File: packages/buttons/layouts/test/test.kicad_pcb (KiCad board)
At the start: 2 copper layers, 8 parts

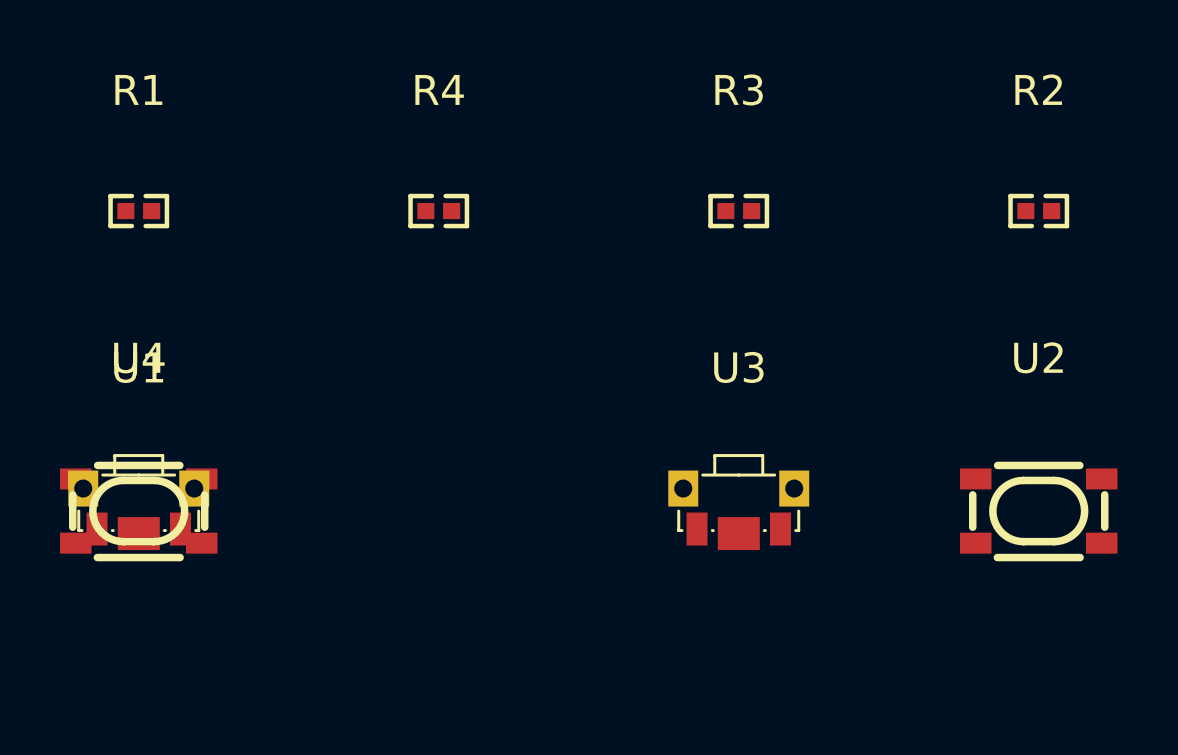
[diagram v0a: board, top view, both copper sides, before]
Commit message: update example and reademe
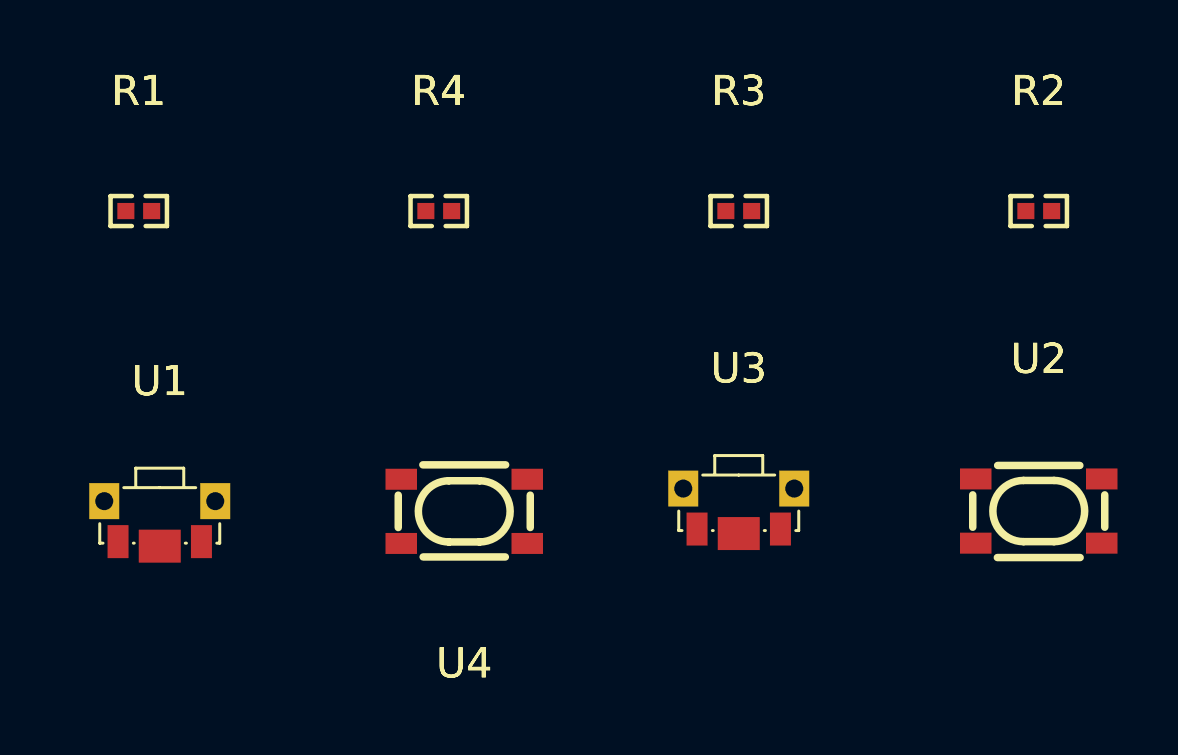
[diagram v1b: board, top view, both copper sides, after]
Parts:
- moved U4 10.9 mm to (10.8, 0.01), turned to 180 degrees
- moved U1 0.82 mm to (0.70, 0.42)
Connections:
- net btn_pullup_vertical-hv renamed hv
- R1 pad 1: net-2 -> net-3
- R2 pad 1: net-1 -> net
- R3 pad 1: net -> net-1
- R4 pad 1: net-3 -> net-2
- U1 pad 1: line -> line-3
- U1 pad 2: net-2 -> net-3
- U2 pad 1: line-3 -> line-1
- U2 pad 2: line-3 -> line-1
- U2 pad 3: net-1 -> net
- U2 pad 4: net-1 -> net
- U3 pad 1: line-2 -> line
- U3 pad 2: net -> net-1
- U4 pad 1: line-1 -> line-2
- U4 pad 2: line-1 -> line-2
- U4 pad 3: net-3 -> net-2
- U4 pad 4: net-3 -> net-2

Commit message: WIP
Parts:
- R1, R2, R3, R4: footprint atopile:R0402-56259e -> UNI_ROYAL_0402WGF1002TCE:R0402
- U1, U3: footprint atopile:KEY-SMD_SKTDLDE010-0426f5 -> ALPSALPINE_SKTDLDE010:KEY-SMD_SKTDLDE010
- U2, U4: footprint atopile:KEY-SMD_4P-L4.2-W3.2-P2.20-LS4.6-a2ccf0 -> ALPSALPINE_SKRPACE010:KEY-SMD_4P-L4.2-W3.2-P2.20-LS4.6
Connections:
- net net renamed _4
- net net-1 renamed _2
- net net-2 renamed unnamed[0]-1
- net net-3 renamed unnamed[0]
- U1 pad 1: line-3 -> line-1
- U2 pad 1: line-1 -> line
- U2 pad 2: line-1 -> line
- U3 pad 1: line -> line-3

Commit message: build all once
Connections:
- net _2 renamed net
- net _4 renamed net-2
- net unnamed[0] renamed net-1
- net unnamed[0]-1 renamed net-3
- U3 pad 1: line-3 -> line-2
- U4 pad 1: line-2 -> line-3
- U4 pad 2: line-2 -> line-3

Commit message: rebuild
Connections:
- net net-3 renamed _3
- R1 pad 1: net-1 -> _2
- R2 pad 1: net-2 -> net
- R3 pad 1: net -> net-1
- U1 pad 1: line-1 -> line-3
- U1 pad 2: net-1 -> _2
- U2 pad 1: line -> line-1
- U2 pad 2: line -> line-1
- U2 pad 3: net-2 -> net
- U2 pad 4: net-2 -> net
- U3 pad 2: net -> net-1
- U4 pad 1: line-3 -> line
- U4 pad 2: line-3 -> line
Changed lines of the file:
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@@
     (net 3 "btn_pulldown_horizontal.btn.footprint.pins[2].net-net")
     (net 4 "btn_pulldown_horizontal-gnd")
-    (net 5 "net-1")
+    (net 5 "_2")
     (net 6 "btn_pulldown_horizontal.btn.footprint.pins[3].net-net")
     (net 7 "btn_pullup_horizontal.btn.footprint.pins[3].net-net")
     (net 8 "line-2")
-    (net 9 "net")
-    (net 10 "line-1")
+    (net 9 "net-1")
+    (net 10 "line-3")
     (net 11 "btn_pullup_horizontal-hv")
     (net 12 "btn_pullup_horizontal.btn.footprint.pins[2].net-net")
-    (net 13 "net-2")
-    (net 14 "line")
-    (net 15 "line-3")
-    (net 16 "net-3")
+    (net 13 "net")
+    (net 14 "line-1")
+    (net 15 "line")
+    (net 16 "_3")
     (footprint "UNI_ROYAL_0402WGF1002TCE:R0402"
         (layer "F.Cu")
@@
             (size 0.57 0.54)
             (layers "F.Cu" "F.Paste" "F.Mask")
-            (net 9 "net")
+            (net 9 "net-1")
         )
         (model "${KIPRJMOD}/../../parts/UNI_ROYAL_0402WGF1002TCE/R0402_L1.0-W0.5-H0.4.step"
@@
             (size 0.7 1.1)
             (layers "F.Cu" "F.Paste" "F.Mask")
-            (net 9 "net")
+            (net 9 "net-1")
         )
         (pad "1" smd rect
@@
             (size 1.05 0.7)
             (layers "F.Cu" "F.Paste" "F.Mask")
-            (net 14 "line")
+            (net 14 "line-1")
         )
         (pad "2" smd rect
@@
             (size 1.05 0.7)
             (layers "F.Cu" "F.Paste" "F.Mask")
-            (net 14 "line")
+            (net 14 "line-1")
         )
         (pad "3" smd rect
@@
             (size 1.05 0.7)
             (layers "F.Cu" "F.Paste" "F.Mask")
-            (net 13 "net-2")
+            (net 13 "net")
         )
         (pad "4" smd rect
@@
             (size 1.05 0.7)
             (layers "F.Cu" "F.Paste" "F.Mask")
-            (net 13 "net-2")
+            (net 13 "net")
         )
         (model "${KIPRJMOD}/../../parts/ALPSALPINE_SKRPACE010/KEY-SMD_4P-L4.2-W3.2-H2.5-LS4.6-P2.2.step"
@@
             (size 0.57 0.54)
             (layers "F.Cu" "F.Paste" "F.Mask")
-            (net 16 "net-3")
+            (net 16 "_3")
         )
         (model "${KIPRJMOD}/../../parts/UNI_ROYAL_0402WGF1002TCE/R0402_L1.0-W0.5-H0.4.step"
@@
             (size 0.7 1.1)
             (layers "F.Cu" "F.Paste" "F.Mask")
-            (net 5 "net-1")
+            (net 5 "_2")
         )
         (pad "1" smd rect
@@
             (size 0.7 1.1)
             (layers "F.Cu" "F.Paste" "F.Mask")
-            (net 10 "line-1")
+            (net 10 "line-3")
         )
         (pad "3" smd rect
@@
             (size 0.57 0.54)
             (layers "F.Cu" "F.Paste" "F.Mask")
-            (net 13 "net-2")
+            (net 13 "net")
         )
         (model "${KIPRJMOD}/../../parts/UNI_ROYAL_0402WGF1002TCE/R0402_L1.0-W0.5-H0.4.step"
@@
             (size 1.05 0.7)
             (layers "F.Cu" "F.Paste" "F.Mask")
-            (net 15 "line-3")
+            (net 15 "line")
         )
         (pad "2" smd rect
@@
             (size 1.05 0.7)
             (layers "F.Cu" "F.Paste" "F.Mask")
-            (net 15 "line-3")
+            (net 15 "line")
         )
         (pad "3" smd rect
@@
             (size 1.05 0.7)
             (layers "F.Cu" "F.Paste" "F.Mask")
-            (net 16 "net-3")
+            (net 16 "_3")
         )
         (pad "4" smd rect
@@
             (size 1.05 0.7)
             (layers "F.Cu" "F.Paste" "F.Mask")
-            (net 16 "net-3")
+            (net 16 "_3")
         )
         (model "${KIPRJMOD}/../../parts/ALPSALPINE_SKRPACE010/KEY-SMD_4P-L4.2-W3.2-H2.5-LS4.6-P2.2.step"
@@
             (size 0.57 0.54)
             (layers "F.Cu" "F.Paste" "F.Mask")
-            (net 5 "net-1")
+            (net 5 "_2")
         )
         (model "${KIPRJMOD}/../../parts/UNI_ROYAL_0402WGF1002TCE/R0402_L1.0-W0.5-H0.4.step"

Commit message: add build_all.py
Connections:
- R3 pad 1: net-1 -> unnamed[1]
- R4 pad 1: _3 -> net-1
- U1 pad 1: line-3 -> line-2
- U2 pad 1: line-1 -> line
- U2 pad 2: line-1 -> line
- U3 pad 1: line-2 -> line-3
- U3 pad 2: net-1 -> unnamed[1]
- U4 pad 1: line -> line-1
- U4 pad 2: line -> line-1
- U4 pad 3: _3 -> net-1
- U4 pad 4: _3 -> net-1
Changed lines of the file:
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@@
     (net 6 "btn_pulldown_horizontal.btn.footprint.pins[3].net-net")
     (net 7 "btn_pullup_horizontal.btn.footprint.pins[3].net-net")
-    (net 8 "line-2")
-    (net 9 "net-1")
-    (net 10 "line-3")
+    (net 8 "line-3")
+    (net 9 "unnamed[1]")
+    (net 10 "line-2")
     (net 11 "btn_pullup_horizontal-hv")
     (net 12 "btn_pullup_horizontal.btn.footprint.pins[2].net-net")
     (net 13 "net")
-    (net 14 "line-1")
-    (net 15 "line")
-    (net 16 "_3")
+    (net 14 "line")
+    (net 15 "line-1")
+    (net 16 "net-1")
     (footprint "UNI_ROYAL_0402WGF1002TCE:R0402"
         (layer "F.Cu")
@@
             (size 0.57 0.54)
             (layers "F.Cu" "F.Paste" "F.Mask")
-            (net 9 "net-1")
+            (net 9 "unnamed[1]")
         )
         (model "${KIPRJMOD}/../../parts/UNI_ROYAL_0402WGF1002TCE/R0402_L1.0-W0.5-H0.4.step"
@@
             (size 0.7 1.1)
             (layers "F.Cu" "F.Paste" "F.Mask")
-            (net 9 "net-1")
+            (net 9 "unnamed[1]")
         )
         (pad "1" smd rect
@@
             (size 0.7 1.1)
             (layers "F.Cu" "F.Paste" "F.Mask")
-            (net 8 "line-2")
+            (net 8 "line-3")
         )
         (pad "3" smd rect
@@
             (size 1.05 0.7)
             (layers "F.Cu" "F.Paste" "F.Mask")
-            (net 14 "line-1")
+            (net 14 "line")
         )
         (pad "2" smd rect
@@
             (size 1.05 0.7)
             (layers "F.Cu" "F.Paste" "F.Mask")
-            (net 14 "line-1")
+            (net 14 "line")
         )
         (pad "3" smd rect
@@
             (size 0.57 0.54)
             (layers "F.Cu" "F.Paste" "F.Mask")
-            (net 16 "_3")
+            (net 16 "net-1")
         )
         (model "${KIPRJMOD}/../../parts/UNI_ROYAL_0402WGF1002TCE/R0402_L1.0-W0.5-H0.4.step"
@@
             (size 0.7 1.1)
             (layers "F.Cu" "F.Paste" "F.Mask")
-            (net 10 "line-3")
+            (net 10 "line-2")
         )
         (pad "3" smd rect
@@
             (size 1.05 0.7)
             (layers "F.Cu" "F.Paste" "F.Mask")
-            (net 15 "line")
+            (net 15 "line-1")
         )
         (pad "2" smd rect
@@
             (size 1.05 0.7)
             (layers "F.Cu" "F.Paste" "F.Mask")
-            (net 15 "line")
+            (net 15 "line-1")
         )
         (pad "3" smd rect
@@
             (size 1.05 0.7)
             (layers "F.Cu" "F.Paste" "F.Mask")
-            (net 16 "_3")
+            (net 16 "net-1")
         )
         (pad "4" smd rect
@@
             (size 1.05 0.7)
             (layers "F.Cu" "F.Paste" "F.Mask")
-            (net 16 "_3")
+            (net 16 "net-1")
         )
         (model "${KIPRJMOD}/../../parts/ALPSALPINE_SKRPACE010/KEY-SMD_4P-L4.2-W3.2-H2.5-LS4.6-P2.2.step"

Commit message: update with 3d models
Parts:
- R1, R2, R3, R4: footprint UNI_ROYAL_0402WGF1002TCE:R0402 -> atopile:R0402-56259e
- U1, U3: footprint ALPSALPINE_SKTDLDE010:KEY-SMD_SKTDLDE010 -> atopile:KEY-SMD_SKTDLDE010-0426f5
- U2, U4: footprint ALPSALPINE_SKRPACE010:KEY-SMD_4P-L4.2-W3.2-P2.20-LS4.6 -> atopile:KEY-SMD_4P-L4.2-W3.2-P2.20-LS4.6-a2ccf0
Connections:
- R1 pad 1: _2 -> net
- R2 pad 1: net -> net-2
- R3 pad 1: unnamed[1] -> net-1
- R4 pad 1: net-1 -> net-3
- U1 pad 1: line-2 -> line
- U1 pad 2: _2 -> net
- U2 pad 1: line -> line-1
- U2 pad 2: line -> line-1
- U2 pad 3: net -> net-2
- U2 pad 4: net -> net-2
- U3 pad 2: unnamed[1] -> net-1
- U4 pad 1: line-1 -> line-2
- U4 pad 2: line-1 -> line-2
- U4 pad 3: net-1 -> net-3
- U4 pad 4: net-1 -> net-3
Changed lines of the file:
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@@
     (net 3 "btn_pulldown_horizontal.btn.footprint.pins[2].net-net")
     (net 4 "btn_pulldown_horizontal-gnd")
-    (net 5 "_2")
+    (net 5 "net")
     (net 6 "btn_pulldown_horizontal.btn.footprint.pins[3].net-net")
     (net 7 "btn_pullup_horizontal.btn.footprint.pins[3].net-net")
     (net 8 "line-3")
-    (net 9 "unnamed[1]")
-    (net 10 "line-2")
+    (net 9 "net-1")
+    (net 10 "line")
     (net 11 "btn_pullup_horizontal-hv")
     (net 12 "btn_pullup_horizontal.btn.footprint.pins[2].net-net")
-    (net 13 "net")
-    (net 14 "line")
-    (net 15 "line-1")
-    (net 16 "net-1")
-    (footprint "UNI_ROYAL_0402WGF1002TCE:R0402"
+    (net 13 "net-2")
+    (net 14 "line-1")
+    (net 15 "line-2")
+    (net 16 "net-3")
+    (footprint "atopile:R0402-56259e"
         (layer "F.Cu")
         (at 20 -10 0)
@@
             )
         )
-        (property "__atopile_lib_fp_hash__" "e8f2e4ec-73af-bd41-8630-d0c87c36316a"
+        (property "__atopile_lib_fp_hash__" "15bb07f0-59a1-3355-2a69-51abf40c8054"
             (at 0 0 0)
             (layer "User.9")
@@
             (size 0.57 0.54)
             (layers "F.Cu" "F.Paste" "F.Mask")
-            (net 9 "unnamed[1]")
-        )
-        (model "${KIPRJMOD}/../../parts/UNI_ROYAL_0402WGF1002TCE/R0402_L1.0-W0.5-H0.4.step"
-            (offset
-                (xyz 0 0 0)
-            )
-            (scale
-                (xyz 1 1 1)
-            )
-            (rotate
-                (xyz 0 0 0)
-            )
+            (net 9 "net-1")
         )
     )
-    (footprint "ALPSALPINE_SKTDLDE010:KEY-SMD_SKTDLDE010"
+    (footprint "atopile:KEY-SMD_SKTDLDE010-0426f5"
         (layer "F.Cu")
         (at 20 0 0)
@@
             )
         )
-        (property "__atopile_lib_fp_hash__" "4c2312aa-ca4b-c936-e1fe-f83dd74b8215"
+        (property "__atopile_lib_fp_hash__" "a723cebe-8ef0-7353-6881-e9482e38bf0e"
             (at 0 0 0)
             (layer "User.9")
@@
             (size 0.7 1.1)
             (layers "F.Cu" "F.Paste" "F.Mask")
-            (net 9 "unnamed[1]")
+            (net 9 "net-1")
         )
         (pad "1" smd rect
@@
             (net 7 "btn_pullup_horizontal.btn.footprint.pins[3].net-net")
         )
-        (model "${KIPRJMOD}/../../parts/ALPSALPINE_SKTDLDE010/KEY-SMD_SKTDLDE010.step"
-            (offset
-                (xyz 0 0 0.5)
-            )
-            (scale
-                (xyz 1 1 1)
-            )
-            (rotate
-                (xyz 0 0 0)
-            )
-        )
     )
-    (footprint "ALPSALPINE_SKRPACE010:KEY-SMD_4P-L4.2-W3.2-P2.20-LS4.6"
+    (footprint "atopile:KEY-SMD_4P-L4.2-W3.2-P2.20-LS4.6-a2ccf0"
         (layer "F.Cu")
         (at 30 0 0)
@@
             )
         )
-        (property "__atopile_lib_fp_hash__" "20086f22-b449-d21b-a0e7-e4e4a199ca49"
+        (property "__atopile_lib_fp_hash__" "2046e8a7-7897-cade-e0dc-8aa03bb6068b"
             (at 0 0 0)
             (layer "User.9")
@@
             (size 1.05 0.7)
             (layers "F.Cu" "F.Paste" "F.Mask")
-            (net 14 "line")
+            (net 14 "line-1")
         )
         (pad "2" smd rect
@@
             (size 1.05 0.7)
             (layers "F.Cu" "F.Paste" "F.Mask")
-            (net 14 "line")
+            (net 14 "line-1")
         )
         (pad "3" smd rect
@@
             (size 1.05 0.7)
             (layers "F.Cu" "F.Paste" "F.Mask")
-            (net 13 "net")
+            (net 13 "net-2")
         )
         (pad "4" smd rect
@@
             (size 1.05 0.7)
             (layers "F.Cu" "F.Paste" "F.Mask")
-            (net 13 "net")
-        )
-        (model "${KIPRJMOD}/../../parts/ALPSALPINE_SKRPACE010/KEY-SMD_4P-L4.2-W3.2-H2.5-LS4.6-P2.2.step"
-            (offset
-                (xyz 0 0 0)
-            )
-            (scale
-                (xyz 1 1 1)
-            )
-            (rotate
-                (xyz 0 0 0)
-            )
+            (net 13 "net-2")
         )
     )
-    (footprint "UNI_ROYAL_0402WGF1002TCE:R0402"
+    (footprint "atopile:R0402-56259e"
         (layer "F.Cu")
         (at 10 -10 0)
@@
             )
         )
-        (property "__atopile_lib_fp_hash__" "e8f2e4ec-73af-bd41-8630-d0c87c36316a"
+        (property "__atopile_lib_fp_hash__" "afcbf7ab-897c-511e-4899-44641277287d"
             (at 0 0 0)
             (layer "User.9")
@@
             (size 0.57 0.54)
             (layers "F.Cu" "F.Paste" "F.Mask")
-            (net 16 "net-1")
-        )
-        (model "${KIPRJMOD}/../../parts/UNI_ROYAL_0402WGF1002TCE/R0402_L1.0-W0.5-H0.4.step"
-            (offset
-                (xyz 0 0 0)
-            )
-            (scale
-                (xyz 1 1 1)
-            )
-            (rotate
-                (xyz 0 0 0)
-            )
+            (net 16 "net-3")
         )
     )
-    (footprint "ALPSALPINE_SKTDLDE010:KEY-SMD_SKTDLDE010"
+    (footprint "atopile:KEY-SMD_SKTDLDE010-0426f5"
         (layer "F.Cu")
         (at 0.7 0.42 0)
@@
             )
         )
-        (property "__atopile_lib_fp_hash__" "4c2312aa-ca4b-c936-e1fe-f83dd74b8215"
+        (property "__atopile_lib_fp_hash__" "e4df4013-dd8f-b4fa-d894-b53e6db9ab2d"
             (at 0 0 0)
             (layer "User.9")
@@
             (size 0.7 1.1)
             (layers "F.Cu" "F.Paste" "F.Mask")
-            (net 5 "_2")
+            (net 5 "net")
         )
         (pad "1" smd rect
@@
             (size 0.7 1.1)
             (layers "F.Cu" "F.Paste" "F.Mask")
-            (net 10 "line-2")
+            (net 10 "line")
         )
         (pad "3" smd rect
@@
             (net 6 "btn_pulldown_horizontal.btn.footprint.pins[3].net-net")
         )
-        (model "${KIPRJMOD}/../../parts/ALPSALPINE_SKTDLDE010/KEY-SMD_SKTDLDE010.step"
-            (offset
-                (xyz 0 0 0.5)
-            )
-            (scale
-                (xyz 1 1 1)
-            )
-            (rotate
-                (xyz 0 0 0)
-            )
-        )
     )
-    (footprint "UNI_ROYAL_0402WGF1002TCE:R0402"
+    (footprint "atopile:R0402-56259e"
         (layer "F.Cu")
         (at 30 -10 0)
@@
             )
         )
-        (property "__atopile_lib_fp_hash__" "e8f2e4ec-73af-bd41-8630-d0c87c36316a"
+        (property "__atopile_lib_fp_hash__" "2064f88c-9f48-673e-9735-9613498797c3"
             (at 0 0 0)
             (layer "User.9")
@@
             (size 0.57 0.54)
             (layers "F.Cu" "F.Paste" "F.Mask")
-            (net 13 "net")
-        )
-        (model "${KIPRJMOD}/../../parts/UNI_ROYAL_0402WGF1002TCE/R0402_L1.0-W0.5-H0.4.step"
-            (offset
-                (xyz 0 0 0)
-            )
-            (scale
-                (xyz 1 1 1)
-            )
-            (rotate
-                (xyz 0 0 0)
-            )
+            (net 13 "net-2")
         )
     )
-    (footprint "ALPSALPINE_SKRPACE010:KEY-SMD_4P-L4.2-W3.2-P2.20-LS4.6"
+    (footprint "atopile:KEY-SMD_4P-L4.2-W3.2-P2.20-LS4.6-a2ccf0"
         (layer "F.Cu")
         (at 10.85 0.01 180)
@@
             )
         )
-        (property "__atopile_lib_fp_hash__" "20086f22-b449-d21b-a0e7-e4e4a199ca49"
+        (property "__atopile_lib_fp_hash__" "39d92071-237d-bbf8-b2c8-d38064b1f8f1"
             (at 0 0 0)
             (layer "User.9")
@@
             (size 1.05 0.7)
             (layers "F.Cu" "F.Paste" "F.Mask")
-            (net 15 "line-1")
+            (net 15 "line-2")
         )
         (pad "2" smd rect
@@
             (size 1.05 0.7)
             (layers "F.Cu" "F.Paste" "F.Mask")
-            (net 15 "line-1")
+            (net 15 "line-2")
         )
         (pad "3" smd rect
@@
             (size 1.05 0.7)
             (layers "F.Cu" "F.Paste" "F.Mask")
-            (net 16 "net-1")
+            (net 16 "net-3")
         )
         (pad "4" smd rect
@@
             (size 1.05 0.7)
             (layers "F.Cu" "F.Paste" "F.Mask")
-            (net 16 "net-1")
-        )
-        (model "${KIPRJMOD}/../../parts/ALPSALPINE_SKRPACE010/KEY-SMD_4P-L4.2-W3.2-H2.5-LS4.6-P2.2.step"
-            (offset
-                (xyz 0 0 0)
-            )
-            (scale
-                (xyz 1 1 1)
-            )
-            (rotate
-                (xyz 0 0 0)
-            )
+            (net 16 "net-3")
         )
     )
-    (footprint "UNI_ROYAL_0402WGF1002TCE:R0402"
+    (footprint "atopile:R0402-56259e"
         (layer "F.Cu")
         (at 0 -10 0)
@@
             )
         )
-        (property "__atopile_lib_fp_hash__" "e8f2e4ec-73af-bd41-8630-d0c87c36316a"
+        (property "__atopile_lib_fp_hash__" "25b24439-7c1b-f15e-f125-7f680f46aa84"
             (at 0 0 0)
             (layer "User.9")
@@
             (size 0.57 0.54)
             (layers "F.Cu" "F.Paste" "F.Mask")
-            (net 5 "_2")
-        )
-        (model "${KIPRJMOD}/../../parts/UNI_ROYAL_0402WGF1002TCE/R0402_L1.0-W0.5-H0.4.step"
-            (offset
-                (xyz 0 0 0)
-            )
-            (scale
-                (xyz 1 1 1)
-            )
-            (rotate
-                (xyz 0 0 0)
-            )
+            (net 5 "net")
         )
     )
